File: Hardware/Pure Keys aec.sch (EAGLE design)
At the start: 58 parts, among them IC1 TL074P, IC2 TL072P, IC5 TL074P, Q2 20MHz, T1 2N3904, U2 LM4040A50IDBZT, U3 328P

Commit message: Slight update
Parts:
- renumbered U$6 to BUT2, U$7 to BUT1
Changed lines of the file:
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@@
 <part name="GLIDE1" library="GMSN" deviceset="9MMPOT" device="" value="rate"/>
 <part name="GLIDE2" library="GMSN" deviceset="9MMPOT" device="" value="rate"/>
-<part name="U$7" library="INSTRUO" deviceset="PB6149L-5" device=""/>
+<part name="BUT1" library="INSTRUO" deviceset="PB6149L-5" device=""/>
 <part name="R55" library="rcl" deviceset="R-US_" device="R0805" value="100K"/>
 <part name="R56" library="rcl" deviceset="R-US_" device="R0805" value="330R"/>
-<part name="U$6" library="INSTRUO" deviceset="PB6149L-5" device=""/>
+<part name="BUT2" library="INSTRUO" deviceset="PB6149L-5" device=""/>
 <part name="R1" library="rcl" deviceset="R-US_" device="R0805" value="100K"/>
 <part name="R2" library="rcl" deviceset="R-US_" device="R0805" value="330R"/>
@@
 <instance part="GLIDE1" gate="G$1" x="12.7" y="35.56" rot="R270"/>
 <instance part="GLIDE2" gate="G$1" x="45.72" y="35.56" rot="R270"/>
-<instance part="U$7" gate="G$1" x="119.38" y="68.58"/>
-<instance part="U$7" gate="G$2" x="119.38" y="50.8" rot="R90"/>
+<instance part="BUT1" gate="G$1" x="119.38" y="68.58"/>
+<instance part="BUT1" gate="G$2" x="119.38" y="50.8" rot="R90"/>
 <instance part="R55" gate="G$1" x="99.06" y="60.96" rot="MR180"/>
 <instance part="R56" gate="G$1" x="132.08" y="50.8" rot="MR0"/>
-<instance part="U$6" gate="G$1" x="119.38" y="30.48"/>
-<instance part="U$6" gate="G$2" x="119.38" y="12.7" rot="R90"/>
+<instance part="BUT2" gate="G$1" x="119.38" y="30.48"/>
+<instance part="BUT2" gate="G$2" x="119.38" y="12.7" rot="R90"/>
 <instance part="R1" gate="G$1" x="99.06" y="22.86" rot="MR180"/>
 <instance part="R2" gate="G$1" x="132.08" y="12.7" rot="MR0"/>
@@
 </segment>
 <segment>
-<pinref part="U$7" gate="G$1" pin="2"/>
+<pinref part="BUT1" gate="G$1" pin="2"/>
 <wire x1="129.54" y1="68.58" x2="134.62" y2="68.58" width="0.1524" layer="91"/>
 <wire x1="134.62" y1="68.58" x2="134.62" y2="71.12" width="0.1524" layer="91"/>
-<pinref part="U$7" gate="G$1" pin="4"/>
+<pinref part="BUT1" gate="G$1" pin="4"/>
 <wire x1="129.54" y1="63.5" x2="134.62" y2="63.5" width="0.1524" layer="91"/>
 <wire x1="134.62" y1="63.5" x2="134.62" y2="68.58" width="0.1524" layer="91"/>
@@
 </segment>
 <segment>
-<pinref part="U$6" gate="G$1" pin="2"/>
+<pinref part="BUT2" gate="G$1" pin="2"/>
 <wire x1="129.54" y1="30.48" x2="134.62" y2="30.48" width="0.1524" layer="91"/>
 <wire x1="134.62" y1="30.48" x2="134.62" y2="33.02" width="0.1524" layer="91"/>
-<pinref part="U$6" gate="G$1" pin="4"/>
+<pinref part="BUT2" gate="G$1" pin="4"/>
 <wire x1="129.54" y1="25.4" x2="134.62" y2="25.4" width="0.1524" layer="91"/>
 <wire x1="134.62" y1="25.4" x2="134.62" y2="30.48" width="0.1524" layer="91"/>
@@
 <net name="BUT1" class="0">
 <segment>
-<pinref part="U$7" gate="G$1" pin="1"/>
+<pinref part="BUT1" gate="G$1" pin="1"/>
 <wire x1="109.22" y1="68.58" x2="104.14" y2="68.58" width="0.1524" layer="91"/>
-<pinref part="U$7" gate="G$1" pin="3"/>
+<pinref part="BUT1" gate="G$1" pin="3"/>
 <wire x1="109.22" y1="63.5" x2="104.14" y2="63.5" width="0.1524" layer="91"/>
 <wire x1="104.14" y1="63.5" x2="104.14" y2="68.58" width="0.1524" layer="91"/>
@@
 <net name="BUTLED1" class="0">
 <segment>
-<pinref part="U$7" gate="G$2" pin="A"/>
+<pinref part="BUT1" gate="G$2" pin="A"/>
 <wire x1="106.68" y1="50.8" x2="116.84" y2="50.8" width="0.1524" layer="91"/>
 <label x="106.68" y="50.8" size="1.778" layer="95" rot="R180"/>
@@
 <net name="N$65" class="0">
 <segment>
-<pinref part="U$7" gate="G$2" pin="C"/>
+<pinref part="BUT1" gate="G$2" pin="C"/>
 <pinref part="R56" gate="G$1" pin="2"/>
 <wire x1="127" y1="50.8" x2="124.46" y2="50.8" width="0.1524" layer="91"/>
@@
 <net name="N$8" class="0">
 <segment>
-<pinref part="U$6" gate="G$2" pin="C"/>
+<pinref part="BUT2" gate="G$2" pin="C"/>
 <pinref part="R2" gate="G$1" pin="2"/>
 <wire x1="127" y1="12.7" x2="124.46" y2="12.7" width="0.1524" layer="91"/>
@@
 <net name="BUT2" class="0">
 <segment>
-<pinref part="U$6" gate="G$1" pin="3"/>
+<pinref part="BUT2" gate="G$1" pin="3"/>
 <wire x1="109.22" y1="25.4" x2="104.14" y2="25.4" width="0.1524" layer="91"/>
 <pinref part="R1" gate="G$1" pin="2"/>
 <wire x1="104.14" y1="25.4" x2="104.14" y2="22.86" width="0.1524" layer="91"/>
-<pinref part="U$6" gate="G$1" pin="1"/>
+<pinref part="BUT2" gate="G$1" pin="1"/>
 <wire x1="109.22" y1="30.48" x2="104.14" y2="30.48" width="0.1524" layer="91"/>
 <wire x1="104.14" y1="30.48" x2="104.14" y2="25.4" width="0.1524" layer="91"/>
@@
 <net name="BUTLED2" class="0">
 <segment>
-<pinref part="U$6" gate="G$2" pin="A"/>
+<pinref part="BUT2" gate="G$2" pin="A"/>
 <wire x1="116.84" y1="12.7" x2="104.14" y2="12.7" width="0.1524" layer="91"/>
 <label x="104.14" y="12.7" size="1.778" layer="95" rot="R180"/>

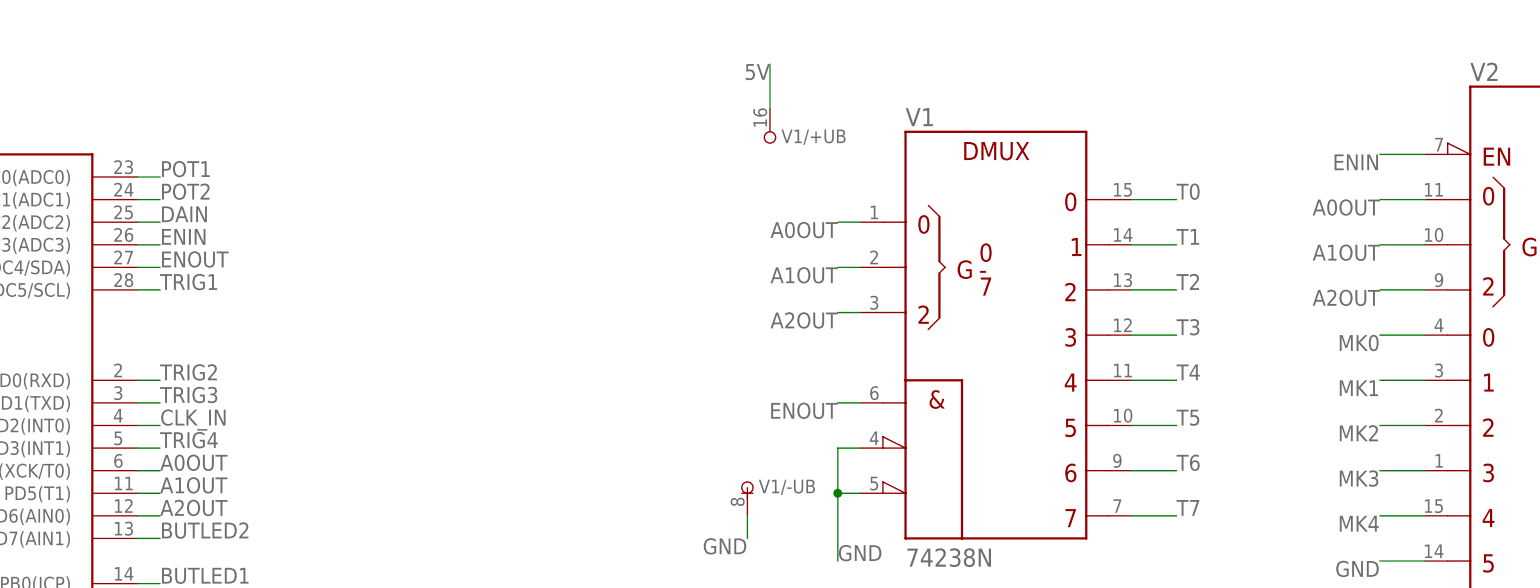
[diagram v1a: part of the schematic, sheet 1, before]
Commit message: Changed MUX/DEMUX connections and removed one POT
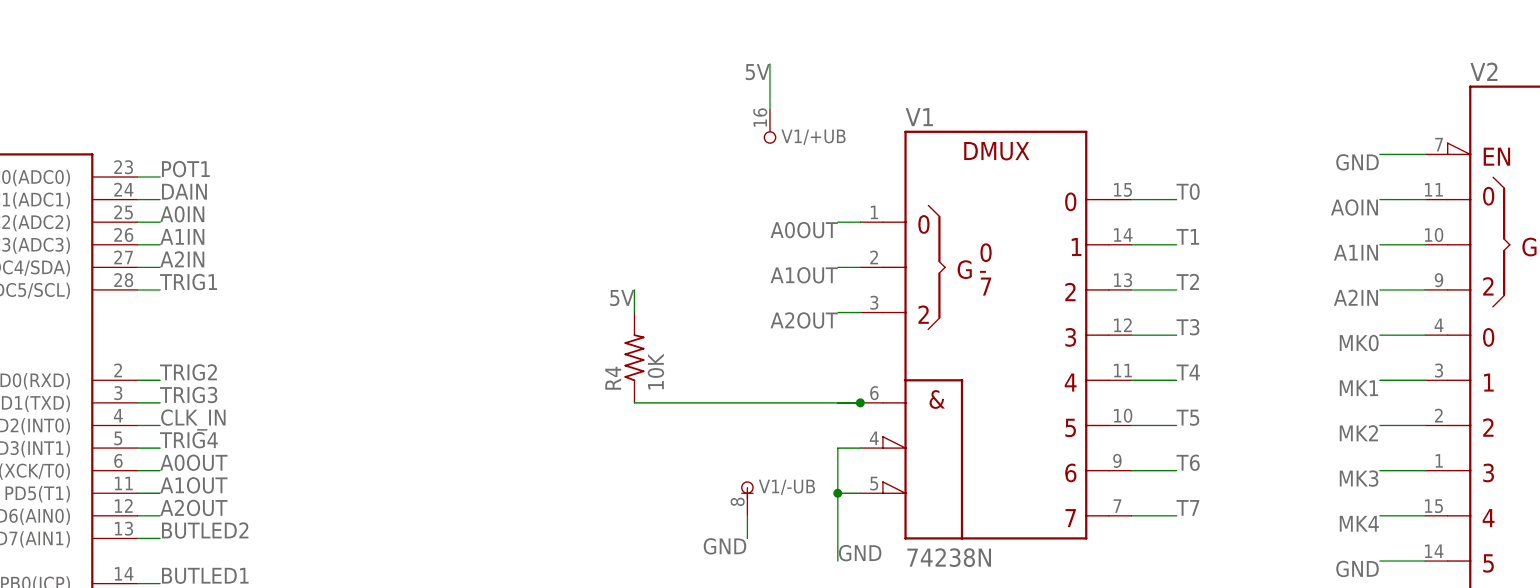
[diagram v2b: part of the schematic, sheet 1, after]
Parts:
- removed GLIDE2: rate, GMSN:9MMPOT
- added R4: 10K, rcl:R-US_R0805
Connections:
- removed net ENIN: U3.PC3(ADC3), V21.!G
- removed net POT2: GLIDE2.2, U3.PC1(ADC1)
- new net A0IN: U3.PC2(ADC2)
- new net A1IN: U3.PC3(ADC3), V21.B
- new net A2IN: U3.PC4(ADC4/SDA), V21.C
- new net AOIN: V21.A
- net 5V: now also R4.2; no longer GLIDE2.1
- net A0OUT: no longer V21.A
- net A1OUT: no longer V21.B
- net A2OUT: no longer V21.C
- net DAIN: now also U3.PC1(ADC1); no longer U3.PC2(ADC2)
- net ENOUT: now also R4.1; no longer U3.PC4(ADC4/SDA)
- net GND: now also V21.!G; no longer GLIDE2.3
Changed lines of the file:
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@@
 <part name="C14" library="rcl" deviceset="C-US" device="C0805K" value="100n"/>
 <part name="GLIDE1" library="GMSN" deviceset="9MMPOT" device="" value="rate"/>
-<part name="GLIDE2" library="GMSN" deviceset="9MMPOT" device="" value="rate"/>
 <part name="BUT1" library="INSTRUO" deviceset="PB6149L-5" device=""/>
 <part name="R55" library="rcl" deviceset="R-US_" device="R0805" value="100K"/>
@@
 <part name="C17" library="rcl" deviceset="C-US" device="C0805K" value="22p"/>
 <part name="C18" library="rcl" deviceset="C-US" device="C0805K" value="22p"/>
+<part name="R4" library="rcl" deviceset="R-US_" device="R0805" value="10K"/>
 </parts>
 <sheets>
@@
 <instance part="V2" gate="/+UB" x="248.92" y="175.26"/>
 <instance part="V2" gate="/-UB" x="251.46" y="114.3"/>
+<instance part="R4" gate="G$1" x="121.92" y="144.78" rot="R90"/>
 </instances>
 <busses>
@@
 <label x="205.74" y="121.92" size="1.778" layer="95" rot="R180"/>
 </segment>
+<segment>
+<pinref part="V2" gate="1" pin="!G"/>
+<wire x1="210.82" y1="167.64" x2="205.74" y2="167.64" width="0.1524" layer="91"/>
+<label x="205.74" y="167.64" size="1.778" layer="95" rot="R180"/>
+</segment>
 </net>
 <net name="RST" class="0">
@@
 <label x="248.92" y="180.34" size="1.778" layer="95"/>
 </segment>
+<segment>
+<pinref part="R4" gate="G$1" pin="2"/>
+<wire x1="121.92" y1="149.86" x2="121.92" y2="152.4" width="0.1524" layer="91"/>
+<label x="121.92" y="152.4" size="1.778" layer="95" rot="R180"/>
+</segment>
 </net>
 <net name="MK4" class="0">
@@
 <pinref part="V1" gate="1" pin="G1"/>
 <wire x1="147.32" y1="139.7" x2="144.78" y2="139.7" width="0.1524" layer="91"/>
-<label x="144.78" y="139.7" size="1.778" layer="95" rot="R180"/>
-</segment>
-<segment>
-<wire x1="66.04" y1="154.94" x2="68.58" y2="154.94" width="0.1524" layer="91"/>
-<label x="68.58" y="154.94" size="1.778" layer="95"/>
-<pinref part="U3" gate="G$1" pin="PC4(ADC4/SDA)"/>
+<pinref part="R4" gate="G$1" pin="1"/>
+<wire x1="121.92" y1="139.7" x2="147.32" y2="139.7" width="0.1524" layer="91"/>
+<junction x="147.32" y="139.7"/>
 </segment>
 </net>
@@
 </segment>
 <segment>
-<pinref part="V2" gate="1" pin="C"/>
-<wire x1="210.82" y1="152.4" x2="205.74" y2="152.4" width="0.1524" layer="91"/>
-<label x="205.74" y="152.4" size="1.778" layer="95" rot="R180"/>
-</segment>
-<segment>
 <wire x1="66.04" y1="127" x2="68.58" y2="127" width="0.1524" layer="91"/>
 <label x="68.58" y="127" size="1.778" layer="95"/>
@@
 </segment>
 <segment>
-<pinref part="V2" gate="1" pin="B"/>
-<wire x1="210.82" y1="157.48" x2="205.74" y2="157.48" width="0.1524" layer="91"/>
-<label x="205.74" y="157.48" size="1.778" layer="95" rot="R180"/>
-</segment>
-<segment>
 <wire x1="66.04" y1="129.54" x2="68.58" y2="129.54" width="0.1524" layer="91"/>
 <label x="68.58" y="129.54" size="1.778" layer="95"/>
@@
 </segment>
 <segment>
-<pinref part="V2" gate="1" pin="A"/>
-<wire x1="210.82" y1="162.56" x2="205.74" y2="162.56" width="0.1524" layer="91"/>
-<label x="205.74" y="162.56" size="1.778" layer="95" rot="R180"/>
-</segment>
-<segment>
 <wire x1="66.04" y1="132.08" x2="68.58" y2="132.08" width="0.1524" layer="91"/>
 <label x="68.58" y="132.08" size="1.778" layer="95"/>
@@
 </segment>
 </net>
-<net name="ENIN" class="0">
-<segment>
-<pinref part="V2" gate="1" pin="!G"/>
-<wire x1="210.82" y1="167.64" x2="205.74" y2="167.64" width="0.1524" layer="91"/>
-<label x="205.74" y="167.64" size="1.778" layer="95" rot="R180"/>
-</segment>
-<segment>
-<wire x1="66.04" y1="157.48" x2="68.58" y2="157.48" width="0.1524" layer="91"/>
-<label x="68.58" y="157.48" size="1.778" layer="95"/>
-<pinref part="U3" gate="G$1" pin="PC3(ADC3)"/>
-</segment>
-</net>
 <net name="DAIN" class="0">
 <segment>
@@
 </segment>
 <segment>
-<wire x1="66.04" y1="160.02" x2="68.58" y2="160.02" width="0.1524" layer="91"/>
-<label x="68.58" y="160.02" size="1.778" layer="95"/>
-<pinref part="U3" gate="G$1" pin="PC2(ADC2)"/>
+<pinref part="U3" gate="G$1" pin="PC1(ADC1)"/>
+<wire x1="66.04" y1="162.56" x2="68.58" y2="162.56" width="0.1524" layer="91"/>
+<label x="68.58" y="162.56" size="1.778" layer="95"/>
 </segment>
 </net>
@@
 <label x="68.58" y="165.1" size="1.778" layer="95"/>
 <pinref part="U3" gate="G$1" pin="PC0(ADC0)"/>
-</segment>
-</net>
-<net name="POT2" class="0">
-<segment>
-<wire x1="66.04" y1="162.56" x2="68.58" y2="162.56" width="0.1524" layer="91"/>
-<label x="68.58" y="162.56" size="1.778" layer="95"/>
-<pinref part="U3" gate="G$1" pin="PC1(ADC1)"/>
 </segment>
 </net>
@@
 <wire x1="66.04" y1="119.38" x2="68.58" y2="119.38" width="0.1524" layer="91"/>
 <label x="68.58" y="119.38" size="1.778" layer="95"/>
+</segment>
+</net>
+<net name="AOIN" class="0">
+<segment>
+<pinref part="V2" gate="1" pin="A"/>
+<wire x1="210.82" y1="162.56" x2="205.74" y2="162.56" width="0.1524" layer="91"/>
+<label x="205.74" y="162.56" size="1.778" layer="95" rot="R180"/>
+</segment>
+</net>
+<net name="A1IN" class="0">
+<segment>
+<pinref part="V2" gate="1" pin="B"/>
+<wire x1="210.82" y1="157.48" x2="205.74" y2="157.48" width="0.1524" layer="91"/>
+<label x="205.74" y="157.48" size="1.778" layer="95" rot="R180"/>
+</segment>
+<segment>
+<pinref part="U3" gate="G$1" pin="PC3(ADC3)"/>
+<wire x1="66.04" y1="157.48" x2="68.58" y2="157.48" width="0.1524" layer="91"/>
+<label x="68.58" y="157.48" size="1.778" layer="95"/>
+</segment>
+</net>
+<net name="A2IN" class="0">
+<segment>
+<pinref part="V2" gate="1" pin="C"/>
+<wire x1="210.82" y1="152.4" x2="205.74" y2="152.4" width="0.1524" layer="91"/>
+<label x="205.74" y="152.4" size="1.778" layer="95" rot="R180"/>
+</segment>
+<segment>
+<pinref part="U3" gate="G$1" pin="PC4(ADC4/SDA)"/>
+<wire x1="66.04" y1="154.94" x2="68.58" y2="154.94" width="0.1524" layer="91"/>
+<label x="68.58" y="154.94" size="1.778" layer="95"/>
+</segment>
+</net>
+<net name="A0IN" class="0">
+<segment>
+<pinref part="U3" gate="G$1" pin="PC2(ADC2)"/>
+<wire x1="66.04" y1="160.02" x2="68.58" y2="160.02" width="0.1524" layer="91"/>
+<label x="68.58" y="160.02" size="1.778" layer="95"/>
 </segment>
 </net>
@@
 <instances>
 <instance part="GLIDE1" gate="G$1" x="12.7" y="35.56" rot="R270"/>
-<instance part="GLIDE2" gate="G$1" x="45.72" y="35.56" rot="R270"/>
 <instance part="BUT1" gate="G$1" x="119.38" y="68.58"/>
 <instance part="BUT1" gate="G$2" x="119.38" y="50.8" rot="R90"/>
@@
 </segment>
 <segment>
-<pinref part="GLIDE2" gate="G$1" pin="3"/>
-<wire x1="45.72" y1="27.94" x2="45.72" y2="30.48" width="0.1524" layer="91"/>
-<label x="45.72" y="27.94" size="1.778" layer="95" rot="R180"/>
-</segment>
-<segment>
 <pinref part="R56" gate="G$1" pin="1"/>
 <wire x1="137.16" y1="50.8" x2="139.7" y2="50.8" width="0.1524" layer="91"/>
@@
 <wire x1="12.7" y1="43.18" x2="12.7" y2="40.64" width="0.1524" layer="91"/>
 <label x="12.7" y="43.18" size="1.778" layer="95"/>
-</segment>
-<segment>
-<pinref part="GLIDE2" gate="G$1" pin="1"/>
-<wire x1="45.72" y1="43.18" x2="45.72" y2="40.64" width="0.1524" layer="91"/>
-<label x="45.72" y="43.18" size="1.778" layer="95"/>
 </segment>
 <segment>
@@
 </segment>
 </net>
-<net name="POT2" class="0">
-<segment>
-<pinref part="GLIDE2" gate="G$1" pin="2"/>
-<wire x1="40.64" y1="35.56" x2="35.56" y2="35.56" width="0.1524" layer="91"/>
-<label x="35.56" y="35.56" size="1.778" layer="95" rot="R180"/>
-</segment>
-</net>

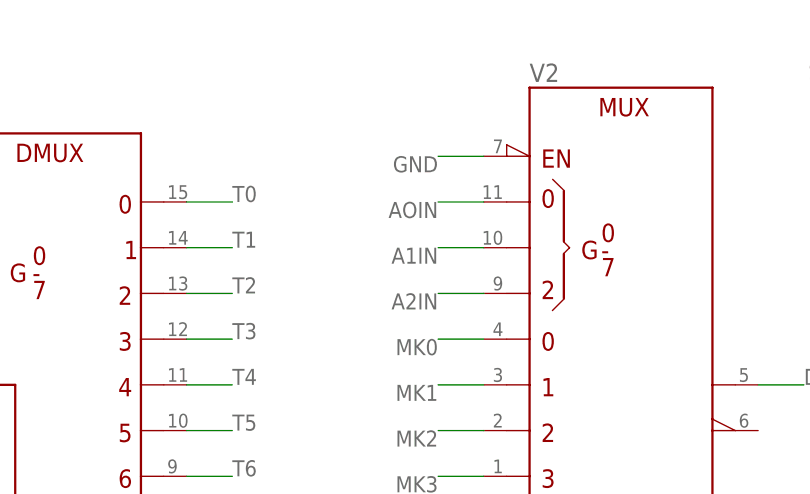
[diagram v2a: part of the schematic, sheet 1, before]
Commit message: added back plane
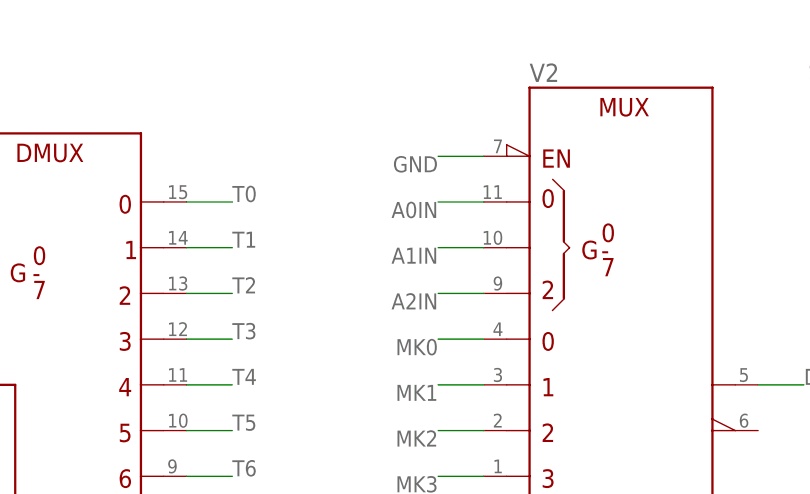
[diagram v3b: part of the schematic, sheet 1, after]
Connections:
- removed net AOIN: V21.A
- net A0IN: now also V21.A
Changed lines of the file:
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@@
-</segment>
-</net>
-<net name="AOIN" class="0">
-<segment>
-<pinref part="V2" gate="1" pin="A"/>
-<wire x1="210.82" y1="162.56" x2="205.74" y2="162.56" width="0.1524" layer="91"/>
-<label x="205.74" y="162.56" size="1.778" layer="95" rot="R180"/>
 </segment>
 </net>
@@
 <label x="68.58" y="160.02" size="1.778" layer="95"/>
 </segment>
+<segment>
+<pinref part="V2" gate="1" pin="A"/>
+<wire x1="210.82" y1="162.56" x2="205.74" y2="162.56" width="0.1524" layer="91"/>
+<label x="205.74" y="162.56" size="1.778" layer="95" rot="R180"/>
+</segment>
 </net>
